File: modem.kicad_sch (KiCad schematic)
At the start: 45 parts, among them Q1 MMBT3904, Q2 MMBT3904, Q3 MMBT3904, Q4 MMBT3904, U3 New Version, U7 SMN-304, U8 SIM7080G

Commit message: Adding ethernet module and more
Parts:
- removed U3: New Version, Rick:dAISy-catcher-11mm, symbol Rick:dAISy-catcher
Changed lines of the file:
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@@
 	(hierarchical_label "GNSS_ANT"
 		(shape bidirectional)
-		(at 270.51 50.8 0)
+		(at 270.51 58.42 0)
 		(effects
 			(font
@@
 					(unit 1)
 				)
-			)
-		)
-	)
-	(symbol
-		(lib_id "Rick:dAISy-catcher")
-		(at 85.09 181.61 0)
-		(unit 1)
-		(body_style 1)
-		(exclude_from_sim no)
-		(in_bom yes)
-		(on_board yes)
-		(in_pos_files yes)
-		(dnp no)
-		(fields_autoplaced yes)
-		(property "Reference" "U3"
-			(at 93.98 180.3399 0)
-			(show_name no)
-			(do_not_autoplace no)
-			(effects
-				(font
-					(size 1.27 1.27)
-				)
-				(justify left)
-			)
-		)
-		(property "Value" "New Version"
-			(at 93.98 182.8799 0)
-			(show_name no)
-			(do_not_autoplace no)
-			(effects
-				(font
-					(size 1.27 1.27)
-				)
-				(justify left)
-			)
-		)
-		(property "Footprint" "Rick:dAISy-catcher-11mm"
-			(at 85.09 181.61 0)
-			(hide yes)
-			(show_name no)
-			(do_not_autoplace no)
-			(effects
-				(font
-					(size 1.27 1.27)
-				)
-			)
-		)
-		(property "Datasheet" ""
-			(at 85.09 181.61 0)
-			(hide yes)
-			(show_name no)
-			(do_not_autoplace no)
-			(effects
-				(font
-					(size 1.27 1.27)
-				)
-			)
-		)
-		(property "Description" ""
-			(at 85.09 181.61 0)
-			(hide yes)
-			(show_name no)
-			(do_not_autoplace no)
-			(effects
-				(font
-					(size 1.27 1.27)
-				)
-			)
-		)
-		(instances
-			(project "AIS-Converter"
-				(path "/af2e2bda-c8b0-494b-9cbc-4303d4ae7608/35a6c23c-94a1-420f-9e5f-a39ff34ffec8"
-					(reference "U3")
-					(unit 1)
-				)

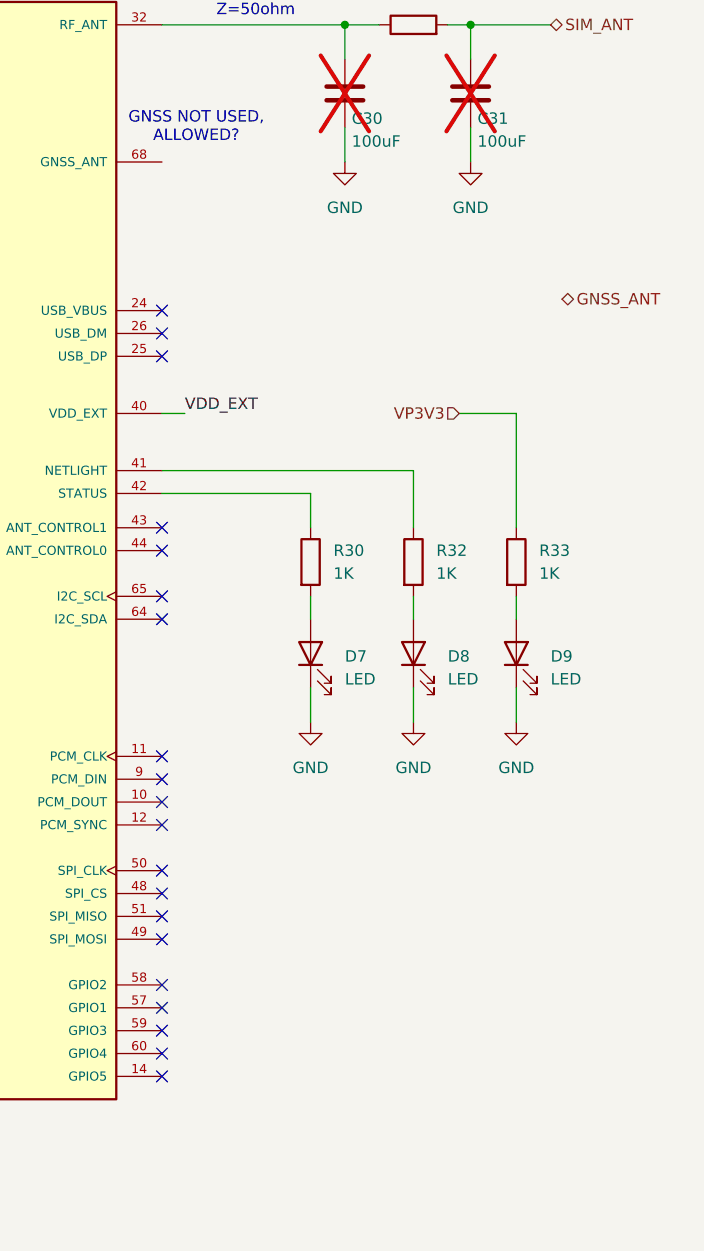
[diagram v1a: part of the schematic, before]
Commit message: NMEA0183 and NMEA2000 schematics
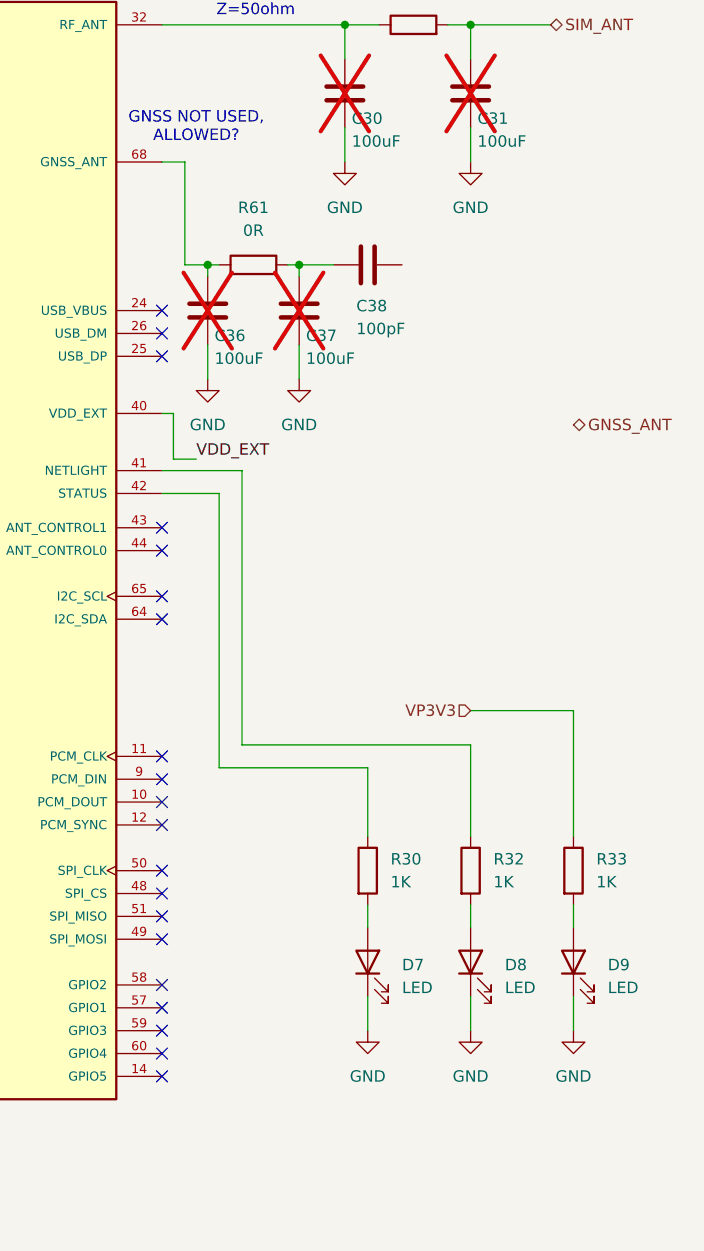
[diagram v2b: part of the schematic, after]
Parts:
- added C36, C37: 100uF, Capacitor_SMD:C_0603_1608Metric, symbol Device:C
- added C38: 100pF, Capacitor_SMD:C_0603_1608Metric, symbol Device:C
- added R61: 0R, Resistor_SMD:R_0603_1608Metric, symbol Device:R
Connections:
- net GND: now also C36.2, C37.2
- net at U8.68 (GNSS_ANT): now also C36.1, R61.1
- new net: C37.1, C38.2, R61.2
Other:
- moved on the sheet: D7, D8, D9, R30, R32, R33

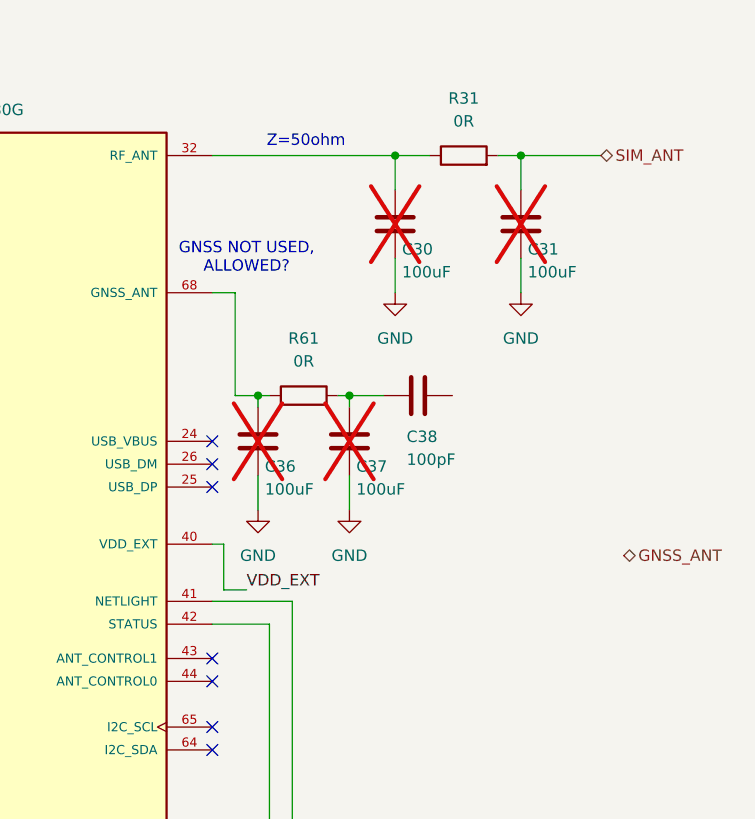
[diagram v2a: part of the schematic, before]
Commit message: Clean up and testpoints
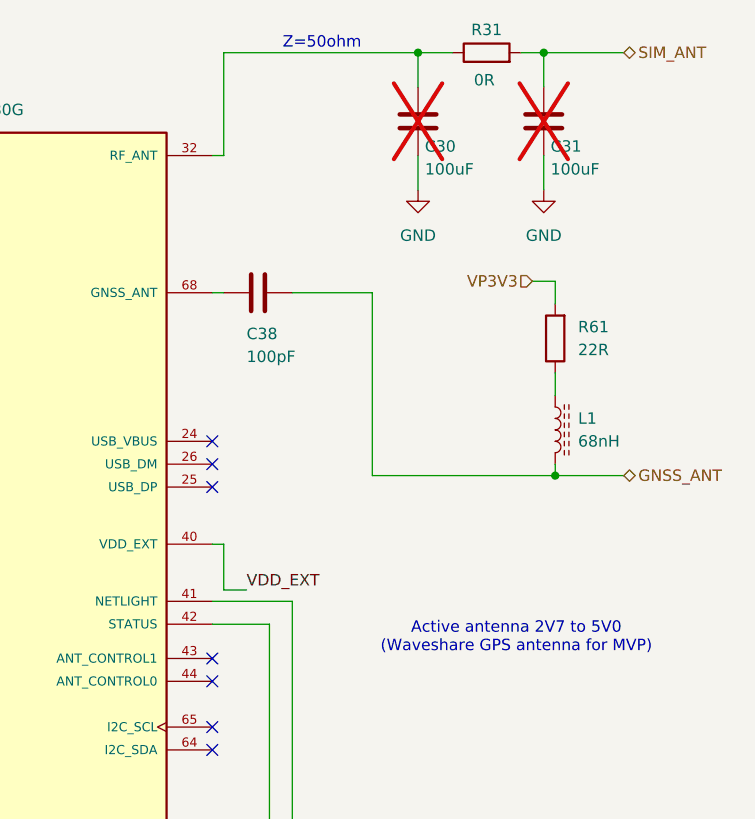
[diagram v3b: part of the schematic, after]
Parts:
- removed C36, C37: 100uF, Capacitor_SMD:C_0603_1608Metric, symbol Device:C
- added L1: 68nH, Inductor_SMD:L_0603_1608Metric, symbol Device:L_Ferrite
- R61: value 0R -> 22R
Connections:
- net GNSS_ANT: now also C38.1, L1.2
- net VBAT: now also R61.2
- net at R61.1: now also L1.1; no longer U8.68 (GNSS_ANT)
- net at C38.2: now also U8.68 (GNSS_ANT); no longer R61.2
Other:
- note added: "Active antenna 2V7 to 5V0 (Waveshare GPS antenna for MVP)"
- note removed: "GNSS NOT USED, ALLOWED?"
- moved on the sheet: C30, C31, C38, R31

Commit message: Power layout started
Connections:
- net at C21.1, R26.1, U7.C3 (CLK): now also D6.5 (K); no longer D6.6 (K)
- net at C20.1, U7.C1 (VCC), U8.18 (SIM_VDD): no longer D6.1 (K)
- net at C22.1, R27.1, U7.C7 (I/O): now also D6.6 (K); no longer D6.5 (K)
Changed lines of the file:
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@@
-	)
-	(junction
-		(at 147.32 128.27)
-		(diameter 0)
-		(color 0 0 0 0)
-	)
-	(junction
-		(at 144.78 125.73)
-		(diameter 0)
-		(color 0 0 0 0)
 	)
 	(junction
@@
 	)
 	(junction
-		(at 149.86 130.81)
-		(diameter 0)
-		(color 0 0 0 0)
-	)
-	(junction
 		(at 248.92 16.51)
 		(diameter 0)
@@
 	)
 	(junction
+		(at 149.86 128.27)
+		(diameter 0)
+		(color 0 0 0 0)
+	)
+	(junction
 		(at 262.89 16.51)
 		(diameter 0)
@@
 	)
 	(junction
+		(at 147.32 130.81)
+		(diameter 0)
+		(color 0 0 0 0)
+	)
+	(junction
 		(at 91.44 142.24)
 		(diameter 0)
@@
 	(wire
 		(pts
-			(xy 149.86 130.81) (xy 149.86 138.43)
-		)
-		(stroke
-			(width 0)
-			(type default)
-		)
-	)
-	(wire
-		(pts
-			(xy 91.44 125.73) (xy 144.78 125.73)
-		)
-		(stroke
-			(width 0)
-			(type default)
-		)
-	)
-	(wire
-		(pts
 			(xy 72.39 39.37) (xy 72.39 88.9)
 		)
@@
 	(wire
 		(pts
-			(xy 123.19 128.27) (xy 147.32 128.27)
+			(xy 149.86 128.27) (xy 149.86 138.43)
 		)
 		(stroke
@@
 	(wire
 		(pts
-			(xy 147.32 128.27) (xy 153.67 128.27)
+			(xy 123.19 128.27) (xy 149.86 128.27)
 		)
 		(stroke
@@
 	(wire
 		(pts
-			(xy 129.54 130.81) (xy 149.86 130.81)
-		)
-		(stroke
-			(width 0)
-			(type default)
-		)
-	)
-	(wire
-		(pts
 			(xy 53.34 83.82) (xy 30.48 83.82)
 		)
@@
 	(wire
 		(pts
+			(xy 147.32 130.81) (xy 147.32 138.43)
+		)
+		(stroke
+			(width 0)
+			(type default)
+		)
+	)
+	(wire
+		(pts
 			(xy 91.44 128.27) (xy 91.44 130.81)
 		)
@@
 	(wire
 		(pts
-			(xy 144.78 125.73) (xy 175.26 125.73)
+			(xy 91.44 125.73) (xy 175.26 125.73)
 		)
 		(stroke
@@
 	(wire
 		(pts
-			(xy 147.32 128.27) (xy 147.32 138.43)
-		)
-		(stroke
-			(width 0)
-			(type default)
-		)
-	)
-	(wire
-		(pts
 			(xy 264.16 52.07) (xy 264.16 54.61)
 		)
@@
 	(wire
 		(pts
-			(xy 149.86 130.81) (xy 160.02 130.81)
+			(xy 129.54 130.81) (xy 147.32 130.81)
 		)
 		(stroke
@@
 	(wire
 		(pts
-			(xy 144.78 125.73) (xy 144.78 138.43)
-		)
-		(stroke
-			(width 0)
-			(type default)
-		)
-	)
-	(wire
-		(pts
 			(xy 29.21 46.99) (xy 33.02 46.99)
 		)
@@
 	(wire
 		(pts
+			(xy 147.32 130.81) (xy 160.02 130.81)
+		)
+		(stroke
+			(width 0)
+			(type default)
+		)
+	)
+	(wire
+		(pts
 			(xy 227.33 43.18) (xy 226.06 43.18)
 		)
@@
 		)
 		(stroke
+			(width 0)
+			(type default)
+		)
+	)
+	(wire
+		(pts
+			(xy 149.86 128.27) (xy 153.67 128.27)
+		)
+		(stroke
